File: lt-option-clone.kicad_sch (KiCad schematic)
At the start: 44 parts, among them P1 Conn_02x13_Odd_Even, U1 65C02, U10 74HCT367, U11 74HCT74, U12 74HCT32, U13 74HCT00, U14 74HCT00, U15 74HCT74, U16 74HCT112, U17 3.6864MHz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

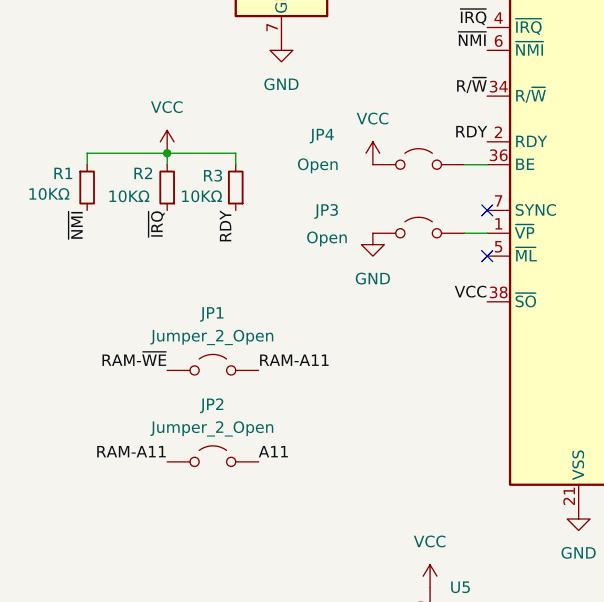
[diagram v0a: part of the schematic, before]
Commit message: Update BOM with resistors
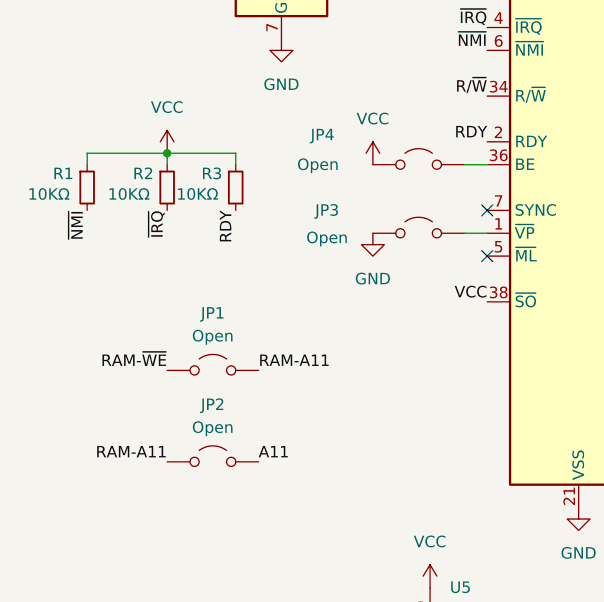
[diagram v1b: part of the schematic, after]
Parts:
- JP1, JP2: value Jumper_2_Open -> Open
- R1, R2, R3: DigiKey Part Number (none) -> 10KEBK-ND; Manufacturer Part Number (none) -> CFR-12JB-52-10K; Mouser Part Number (none) -> 603-CFR-12JB-52-10K
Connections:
- net RDY: now also R3.2; no longer R3.1
- net VCC: now also R2.1, R3.1; no longer R2.2, R3.2
- net ~{IRQ}: now also R2.2; no longer R2.1
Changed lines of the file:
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@@
 	)
 	(symbol
-		(lib_id "Device:R_Small")
-		(at 27.94 67.31 180)
-		(unit 1)
-		(exclude_from_sim no)
-		(in_bom yes)
-		(on_board yes)
-		(dnp no)
-		(property "Reference" "R2"
-			(at 24.13 65.786 0)
-			(effects
-				(font
-					(size 1.27 1.27)
-				)
-				(justify right)
-			)
-		)
-		(property "Value" "10KΩ"
-			(at 21.336 68.326 0)
-			(effects
-				(font
-					(size 1.27 1.27)
-				)
-				(justify right)
-			)
-		)
-		(property "Footprint" "Resistor_THT:R_Axial_DIN0207_L6.3mm_D2.5mm_P7.62mm_Horizontal"
-			(at 27.94 67.31 0)
-			(effects
-				(font
-					(size 1.27 1.27)
-				)
-				(hide yes)
-			)
-		)
-		(property "Datasheet" "~"
-			(at 27.94 67.31 0)
-			(effects
-				(font
-					(size 1.27 1.27)
-				)
-				(hide yes)
-			)
-		)
-		(property "Description" "Resistor, small symbol"
-			(at 27.94 67.31 0)
-			(effects
-				(font
-					(size 1.27 1.27)
-				)
-				(hide yes)
-			)
-		)
-		(property "Arrow Part Number" ""
-			(at 27.94 67.31 0)
-			(effects
-				(font
-					(size 1.27 1.27)
-				)
-				(hide yes)
-			)
-		)
-		(property "Arrow Price/Stock" ""
-			(at 27.94 67.31 0)
-			(effects
-				(font
-					(size 1.27 1.27)
-				)
-				(hide yes)
-			)
-		)
-		(property "Digikey Part Number" ""
-			(at 27.94 67.31 0)
-			(effects
-				(font
-					(size 1.27 1.27)
-				)
-				(hide yes)
-			)
-		)
-		(property "Manufacturer_Name" ""
-			(at 27.94 67.31 0)
-			(effects
-				(font
-					(size 1.27 1.27)
-				)
-				(hide yes)
-			)
-		)
-		(property "Manufacturer_Part_Number" ""
-			(at 27.94 67.31 0)
-			(effects
-				(font
-					(size 1.27 1.27)
-				)
-				(hide yes)
-			)
-		)
-		(property "Mouser Price/Stock" ""
-			(at 27.94 67.31 0)
-			(effects
-				(font
-					(size 1.27 1.27)
-				)
-				(hide yes)
-			)
-		)
-		(property "DigiKey Number" ""
-			(at 27.94 67.31 0)
-			(effects
-				(font
-					(size 1.27 1.27)
-				)
-				(hide yes)
-			)
-		)
-		(property "Mouser Number" ""
-			(at 27.94 67.31 0)
-			(effects
-				(font
-					(size 1.27 1.27)
-				)
-				(hide yes)
-			)
-		)
-		(pin "2"
-		)
-		(pin "1"
-		)
-		(instances
-			(project "lt-option-clone"
-				(path "/b202edd9-fece-42bd-ac83-72150a0b671a"
-					(reference "R2")
-					(unit 1)
-				)
-			)
-		)
-	)
-	(symbol
 		(lib_id "74xx:74LS00")
 		(at 181.61 218.44 0)
@@
 			)
 		)
-		(property "Value" "Jumper_2_Open"
+		(property "Value" "Open"
 			(at 33.02 83.82 0)
 			(effects
@@
 	(symbol
 		(lib_id "Device:R_Small")
-		(at 35.56 67.31 180)
+		(at 35.56 67.31 0)
 		(unit 1)
 		(exclude_from_sim no)
@@
 		(dnp no)
 		(property "Reference" "R3"
-			(at 33.02 66.04 0)
+			(at 31.75 65.786 0)
 			(effects
 				(font
 					(size 1.27 1.27)
 				)
+				(justify left)
 			)
 		)
 		(property "Value" "10KΩ"
-			(at 31.75 68.326 0)
+			(at 28.956 68.072 0)
 			(effects
 				(font
 					(size 1.27 1.27)
 				)
+				(justify left)
 			)
 		)
@@
 			)
 		)
-		(property "Arrow Part Number" ""
-			(at 35.56 67.31 0)
-			(effects
-				(font
-					(size 1.27 1.27)
-				)
-				(hide yes)
-			)
-		)
-		(property "Arrow Price/Stock" ""
-			(at 35.56 67.31 0)
-			(effects
-				(font
-					(size 1.27 1.27)
-				)
-				(hide yes)
-			)
-		)
-		(property "Digikey Part Number" ""
-			(at 35.56 67.31 0)
-			(effects
-				(font
-					(size 1.27 1.27)
-				)
-				(hide yes)
-			)
-		)
-		(property "Manufacturer_Name" ""
+		(property "DigiKey Part Number" "10KEBK-ND"
 			(at 35.56 67.31 0)
 			(effects
@@
 			)
 		)
-		(property "Manufacturer_Part_Number" ""
+		(property "Manufacturer Part Number" "CFR-12JB-52-10K"
 			(at 35.56 67.31 0)
 			(effects
@@
 			)
 		)
-		(property "Mouser Price/Stock" ""
-			(at 35.56 67.31 0)
-			(effects
-				(font
-					(size 1.27 1.27)
-				)
-				(hide yes)
-			)
-		)
-		(property "DigiKey Number" ""
-			(at 35.56 67.31 0)
-			(effects
-				(font
-					(size 1.27 1.27)
-				)
-				(hide yes)
-			)
-		)
-		(property "Mouser Number" ""
+		(property "Mouser Part Number" "603-CFR-12JB-52-10K"
 			(at 35.56 67.31 0)
 			(effects
@@
 			)
 		)
-		(property "Arrow Part Number" ""
-			(at 19.05 67.31 0)
-			(effects
-				(font
-					(size 1.27 1.27)
-				)
-				(hide yes)
-			)
-		)
-		(property "Arrow Price/Stock" ""
+		(property "DigiKey Part Number" "10KEBK-ND"
 			(at 19.05 67.31 0)
 			(effects
@@
 			)
 		)
-		(property "Digikey Part Number" ""
+		(property "Manufacturer Part Number" "CFR-12JB-52-10K"
 			(at 19.05 67.31 0)
 			(effects
@@
 			)
 		)
-		(property "Manufacturer_Name" ""
-			(at 19.05 67.31 0)
-			(effects
-				(font
-					(size 1.27 1.27)
-				)
-				(hide yes)
-			)
-		)
-		(property "Manufacturer_Part_Number" ""
-			(at 19.05 67.31 0)
-			(effects
-				(font
-					(size 1.27 1.27)
-				)
-				(hide yes)
-			)
-		)
-		(property "Mouser Price/Stock" ""
-			(at 19.05 67.31 0)
-			(effects
-				(font
-					(size 1.27 1.27)
-				)
-				(hide yes)
-			)
-		)
-		(property "DigiKey Number" ""
-			(at 19.05 67.31 0)
-			(effects
-				(font
-					(size 1.27 1.27)
-				)
-				(hide yes)
-			)
-		)
-		(property "Mouser Number" ""
+		(property "Mouser Part Number" "603-CFR-12JB-52-10K"
 			(at 19.05 67.31 0)
 			(effects
@@
 	)
 	(symbol
+		(lib_id "Device:R_Small")
+		(at 27.94 67.31 0)
+		(unit 1)
+		(exclude_from_sim no)
+		(in_bom yes)
+		(on_board yes)
+		(dnp no)
+		(property "Reference" "R2"
+			(at 24.13 65.786 0)
+			(effects
+				(font
+					(size 1.27 1.27)
+				)
+				(justify left)
+			)
+		)
+		(property "Value" "10KΩ"
+			(at 21.336 68.072 0)
+			(effects
+				(font
+					(size 1.27 1.27)
+				)
+				(justify left)
+			)
+		)
+		(property "Footprint" "Resistor_THT:R_Axial_DIN0207_L6.3mm_D2.5mm_P7.62mm_Horizontal"
+			(at 27.94 67.31 0)
+			(effects
+				(font
+					(size 1.27 1.27)
+				)
+				(hide yes)
+			)
+		)
+		(property "Datasheet" "~"
+			(at 27.94 67.31 0)
+			(effects
+				(font
+					(size 1.27 1.27)
+				)
+				(hide yes)
+			)
+		)
+		(property "Description" "Resistor, small symbol"
+			(at 27.94 67.31 0)
+			(effects
+				(font
+					(size 1.27 1.27)
+				)
+				(hide yes)
+			)
+		)
+		(property "DigiKey Part Number" "10KEBK-ND"
+			(at 27.94 67.31 0)
+			(effects
+				(font
+					(size 1.27 1.27)
+				)
+				(hide yes)
+			)
+		)
+		(property "Manufacturer Part Number" "CFR-12JB-52-10K"
+			(at 27.94 67.31 0)
+			(effects
+				(font
+					(size 1.27 1.27)
+				)
+				(hide yes)
+			)
+		)
+		(property "Mouser Part Number" "603-CFR-12JB-52-10K"
+			(at 27.94 67.31 0)
+			(effects
+				(font
+					(size 1.27 1.27)
+				)
+				(hide yes)
+			)
+		)
+		(pin "2"
+		)
+		(pin "1"
+		)
+		(instances
+			(project "lt-option-clone"
+				(path "/b202edd9-fece-42bd-ac83-72150a0b671a"
+					(reference "R2")
+					(unit 1)
+				)
+			)
+		)
+	)
+	(symbol
 		(lib_id "74xx:74LS138")
 		(at 208.28 127 0)
@@
 			)
 		)
-		(property "Value" "Jumper_2_Open"
+		(property "Value" "Open"
 			(at 33.02 93.98 0)
 			(effects

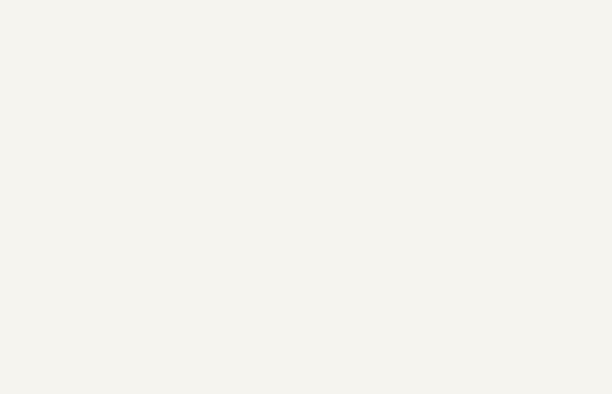
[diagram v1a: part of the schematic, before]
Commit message: Add note about ground wire, add standoffs to BOM
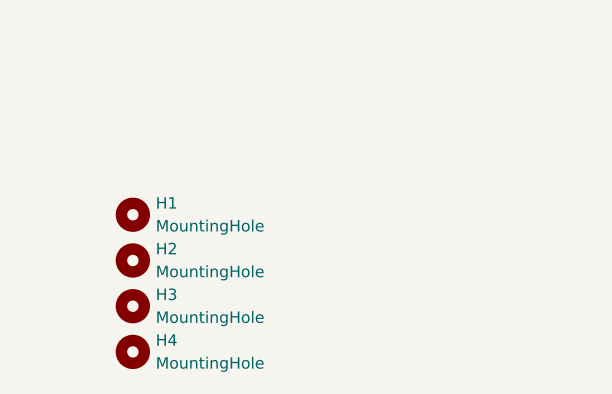
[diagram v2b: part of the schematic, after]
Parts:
- added H1, H2, H3, H4: MountingHole, symbol Mechanical:MountingHole
